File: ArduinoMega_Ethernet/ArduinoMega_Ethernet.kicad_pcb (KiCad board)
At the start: 2 copper layers, 101.6 x 53.3 mm, 120 parts, among them J1 RJ45_Amphenol_RJMG1BD3B8K1ANR, J11 Micro_SD_Card_Det_Hirose_DM3AT, J2 SD_DET_JUMP, J3 IMU_INT1_JUMP, J4 IMU_INT2_JUMP, J5 ETHER_INT_JUMP, J6 RTC_MFP_JUMP, J7 EXT_3V3_I2C, J9 PROGRAM_POWER_USBC, SW1 SW_Push, U1 ATmega2560-16A, U10 TXS0108EPW, U2 CH340C, U3 ISM330DHCX, U4 W5500, U5 AP63205WU, U6 AP63203WU, U7 SE050C2HQ1, U8 AP22804AW5, U9 MCP7940N-xST, Y1 16Mhz, Y2 25Mhz, Y3 32.768kHz

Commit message: w6100 manufacturing and project files
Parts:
- removed C36: 10uF, Capacitor_SMD:C_0805_2012Metric_Pad1.18x1.45mm_HandSolder
- removed D3, D5: LED, LED_SMD:LED_0603_1608Metric
- removed J1: RJ45_Amphenol_RJMG1BD3B8K1ANR, Connector_RJ:RJ45_Amphenol_RJMG1BD3B8K1ANR
- removed JP1: PMODE1, Jumper:SolderJumper-3_P1.3mm_Bridged12_Pad1.0x1.5mm
- removed JP2: PMODE0, Jumper:SolderJumper-3_P1.3mm_Bridged12_Pad1.0x1.5mm
- removed JP3: PMODE2, Jumper:SolderJumper-3_P1.3mm_Bridged12_Pad1.0x1.5mm
- removed R17, R19: 330R, Resistor_SMD:R_0603_1608Metric
- removed R21: 12.4k, Resistor_SMD:R_0603_1608Metric
- removed R22: 10R, Resistor_SMD:R_0603_1608Metric
- removed R24, R26: 82R, Resistor_SMD:R_0603_1608Metric
- removed U4: W5500, Package_QFP:LQFP-48_7x7mm_P0.5mm
- added C50: 100nF, Capacitor_SMD:C_0603_1608Metric, F.Cu at (121.4, 93.0)
- added FB3: FerriteBead_Small, Inductor_SMD:L_0603_1608Metric, F.Cu at (134.8, 100.6)
- added FB4: FerriteBead_Small, Inductor_SMD:L_0603_1608Metric, F.Cu at (140.9, 100.6)
- added IC1: W6100L, EXT_ETHERNET:QFP50P900X900X160-48N, F.Cu at (133.7, 92.2)
- added P1: RB1-125BAG1A, EXT_ETHERNET:WIZNET_RB1-125BAG1A, F.Cu at (108.5, 92.8)
- added R33: 12.3k, Resistor_SMD:R_0603_1608Metric, F.Cu at (125.4, 101.0)
- added R35: 49.9R, Resistor_SMD:R_0603_1608Metric, F.Cu at (121.4, 87.0)
- added R36: 49.9R, Resistor_SMD:R_0603_1608Metric, F.Cu at (121.4, 90.0)
- C15, C16: value 6.8nF -> 100nF
- C17: value 22nF -> 100nF
- C19, C22: value 10nF -> 100nF
- C21: value 4.7uF -> 100nF; footprint Capacitor_SMD:C_0805_2012Metric_Pad1.18x1.45mm_HandSolder -> Capacitor_SMD:C_0603_1608Metric
- R18, R20: value 330R -> 470R
- R23, R25: value 49R -> 49.9R
- R27, R28, R29, R30: value 33R -> 3.3R
- moved C32 21.5 mm to (126.5, 87.1), turned to 180 degrees
- moved C16 20.7 mm to (141.7, 97.0), turned to 0 degrees
- moved C15 19.9 mm to (140.6, 89.6), turned to 0 degrees
- moved C25 19.3 mm to (126.5, 91.0), turned to 180 degrees
- moved R20 19.2 mm to (121.4, 82.3)
- moved C30 18.3 mm to (127.3, 101.6), turned to 0 degrees
- moved C28 16.1 mm to (129.9, 101.6)
- moved C34 15.3 mm to (133.3, 100.6), turned to -90 degrees
- moved Y2 14.2 mm to (128.9, 99.3), turned to 0 degrees
- moved R25 11.4 mm to (121.4, 99.0)
- moved R34 11.0 mm to (128.7, 96.6), turned to 0 degrees
- moved C26 11.0 mm to (131.8, 100.6), turned to -90 degrees
- moved C22 10.6 mm to (126.5, 93.2), turned to 180 degrees
- moved R23 10.1 mm to (121.4, 96.0)
- moved C27 8.83 mm to (139.3, 100.6), turned to -90 degrees
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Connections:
- C15 pad 1: Net-(C15-Pad1) -> +3V3
- C15 pad 2: Net-(J1-RD+) -> GND
- C16 pad 1: Net-(C16-Pad1) -> +3V3
- C16 pad 2: Net-(J1-RD-) -> GND
- C19 pad 1: Net-(J1-RCT) -> Net-(C19-Pad1)
- C21 pad 1: Net-(U4-TOCAP) -> /PWRandPRG/3V3_ANA
- C22 pad 1: Net-(U4-1V2O) -> /PWRandPRG/3V3_ANA
- C25 pad 1: +3V3 -> /PWRandPRG/1V2_ANA
- C26 pad 1: +3V3 -> /PWRandPRG/1V2_DIG
- C27 pad 1: +3V3 -> /PWRandPRG/1V2_DIG
- C29 pad 1: +3V3 -> /PWRandPRG/1V2_DIG
- C32 pad 1: +3V3 -> /PWRandPRG/1V2_DIG
- C34 pad 1: +3V3 -> /PWRandPRG/1V2_OUT
- FB2 pad 1: +3V3 -> /PWRandPRG/3V3_ANA
- FB2 pad 2: Net-(FB2-Pad2) -> +3V3
- R18 pad 1: GND -> /PWRandPRG/ACT_LED
- R20 pad 1: GND -> /PWRandPRG/LINK_LED
- R23 pad 1: Net-(FB2-Pad2) -> Net-(P1-RD-)
- R23 pad 2: Net-(J1-TD+) -> Net-(C19-Pad1)
- R25 pad 1: Net-(FB2-Pad2) -> Net-(P1-RD+)
- R25 pad 2: Net-(J1-TD-) -> Net-(C19-Pad1)
- R27 pad 2: Net-(J1-TD-) -> Net-(P1-TD-)
- R28 pad 2: Net-(J1-TD+) -> Net-(P1-TD+)
- R29 pad 2: Net-(C16-Pad1) -> Net-(P1-RD-)
- R30 pad 2: Net-(C15-Pad1) -> Net-(P1-RD+)
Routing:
- net Net-(FB2-Pad2): track 50.5 -> 0.00 mm, vias 9 -> 0
- net /PWRandPRG/1V2_DIG: track 0.00 -> 45.3 mm, vias 0 -> 4
- net /PWRandPRG/LINK_LED: track 55.5 -> 24.5 mm, vias 2 -> 0
- net /PWRandPRG/ACT_LED: track 51.3 -> 23.2 mm, vias 0 -> 2
- net GND: track 67.1 -> 39.5 mm, vias 146 -> 137
- net +5V: track 282.3 -> 257.4 mm, vias 10 -> 8
- net /PWRandPRG/1V2_ANA: track 0.00 -> 18.9 mm, vias 0 -> 2
- net /PWRandPRG/1V2_OUT: track 0.00 -> 18.0 mm, vias 0 -> 2
- net /PWRandPRG/3V3_ANA: track 0.00 -> 17.1 mm
- net +3V3: track 270.5 -> 255.2 mm, vias 7 -> 4
- net Net-(J1-TD+): track 14.7 -> 0.00 mm
- net Net-(C16-Pad1): track 13.7 -> 0.00 mm
- net Net-(J1-RCT): track 12.0 -> 0.00 mm
- net Net-(J1-RD+): track 11.3 -> 0.00 mm
- net Net-(P1-PadL2): track 17.6 -> 28.8 mm
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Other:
- board text added: "Rev1.0 5-26-2025"
- board text removed: "GND PMD 3V3"
- board text removed: "Rev1.0 5-22-2025"

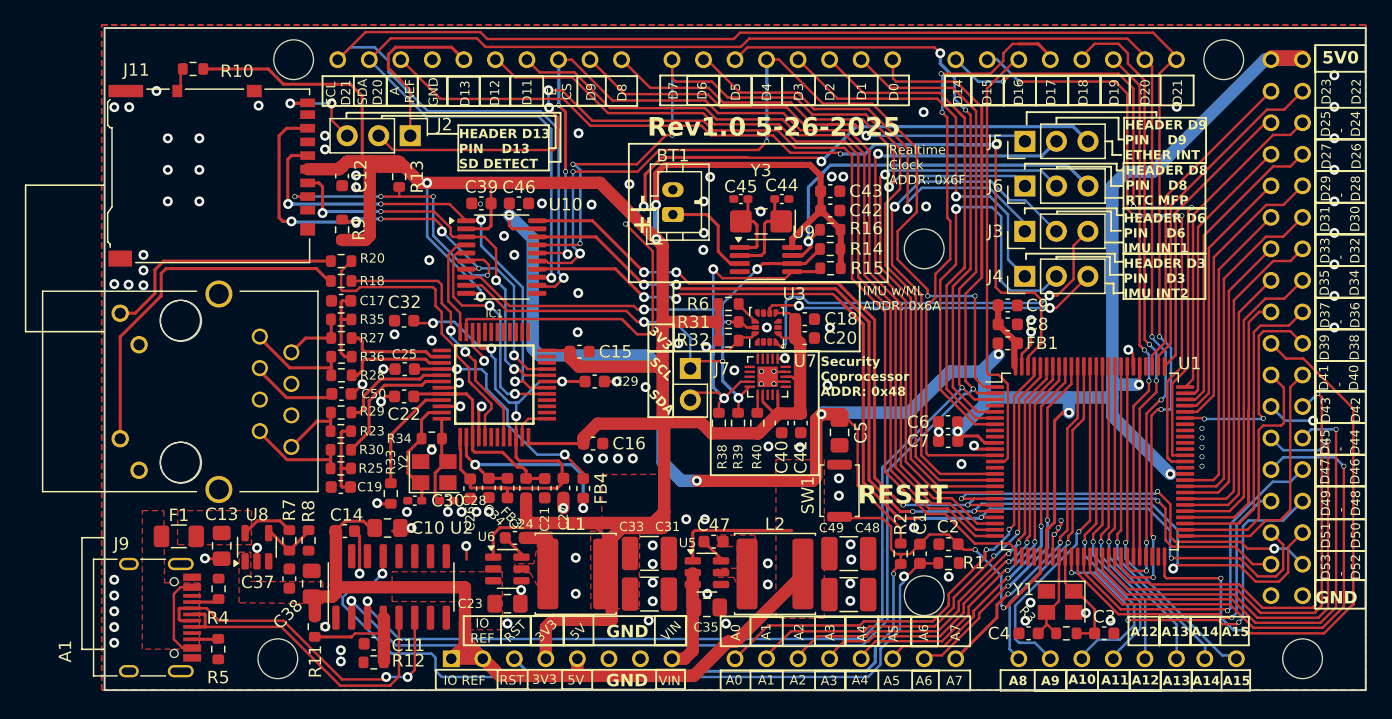
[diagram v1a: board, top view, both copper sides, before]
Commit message: bom and component sizing
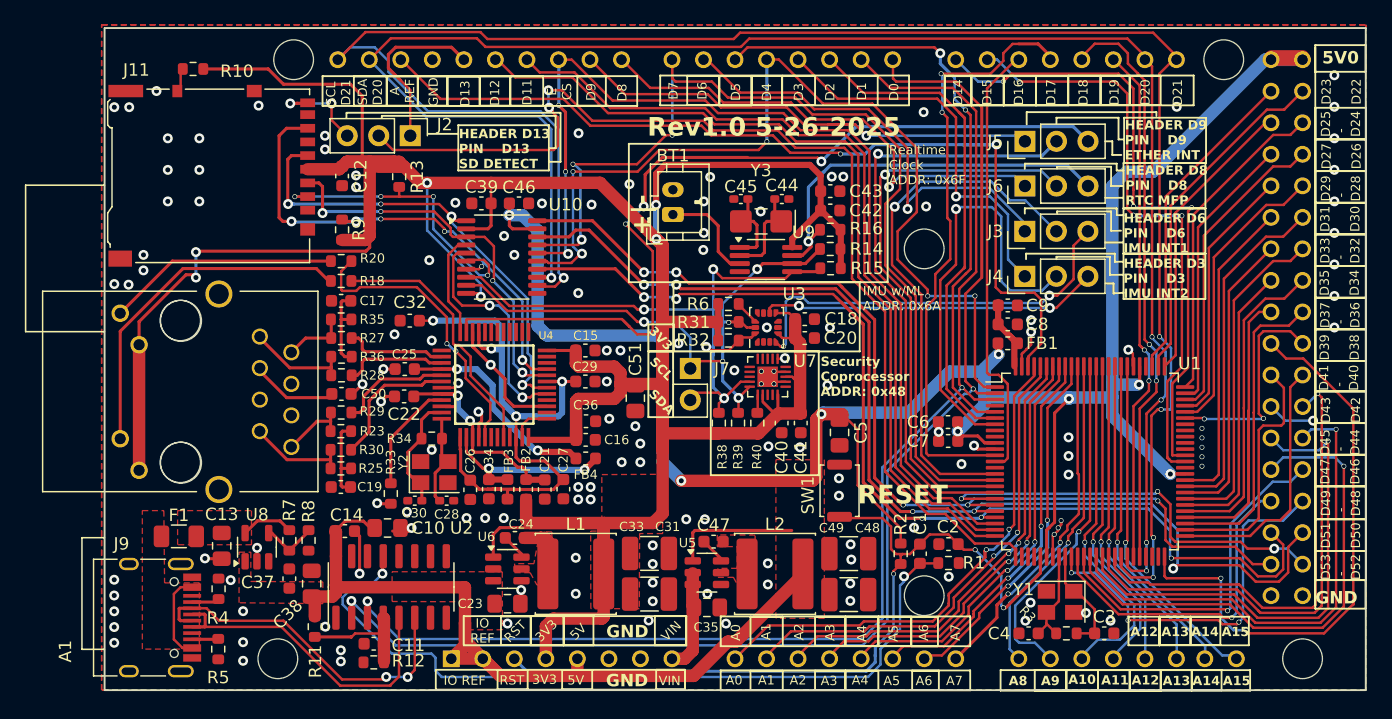
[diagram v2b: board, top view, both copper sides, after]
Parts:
- added C36: 1uF, Capacitor_SMD:C_0603_1608Metric, F.Cu at (141.1, 95.2)
- added C51: 10uF, Capacitor_SMD:C_0805_2012Metric_Pad1.18x1.45mm_HandSolder, F.Cu at (145.1, 93.3)
- moved FB4 2.42 mm to (141.1, 98.2), turned to 0 degrees
- moved C29 0.75 mm to (141.1, 92.0)
- moved C16 0.67 mm to (141.1, 96.7)
- moved C15 0.49 mm to (141.1, 89.5)
- moved C32 0.45 mm to (126.9, 87.1)
- moved C21 0.10 mm to (137.8, 100.7)
- moved C26 0.10 mm to (131.8, 100.7)
- moved C27 0.10 mm to (139.3, 100.7)
- moved C34 0.10 mm to (133.3, 100.7)
- moved FB3 0.10 mm to (134.8, 100.7)
- moved FB2 0.09 mm to (136.3, 100.7)
- renumbered P1 to J1, IC1 to U4
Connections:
- J1 pad L1: GND -> +3V3
- J1 pad L3: GND -> +3V3
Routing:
- net +3V3: track 255.2 -> 305.8 mm, vias 4 -> 6
- net GND: track 39.5 -> 45.2 mm, vias 137 -> 144
- net /PWRandPRG/1V2_DIG: track 45.3 -> 48.5 mm
- net /PWRandPRG/1V2_OUT: track 18.0 -> 15.8 mm
- net /PWRandPRG/ACT_LED: track 23.2 -> 21.1 mm, vias 2 -> 0
- net /PWRandPRG/1V2_ANA: track 18.9 -> 17.4 mm
- net Net-(J1-PadL4): track 19.8 -> 18.7 mm
- net Net-(J1-PadL2): track 28.8 -> 28.0 mm
- net /PWRandPRG/LINK_LED: track 24.5 -> 23.7 mm, vias 0 -> 2
- net /PWRandPRG/3V3_ANA: track 17.1 -> 16.6 mm, vias 0 -> 2
